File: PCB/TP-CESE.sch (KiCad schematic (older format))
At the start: 39 parts, among them J1 Screw_Terminal_01x04, J3 Screw_Terminal_01x02, J4 Conn_01x05_Male, J5 test, Q1 IRF540N, Q2 IRF540N, Q3 IRF540N, Q4 IRF540N, U1 4N25, U2 4N25, U3 4N25, U4 4N25, U5 ADS1015IDGS, X1 Conn_Poncho2P_2x_20x2

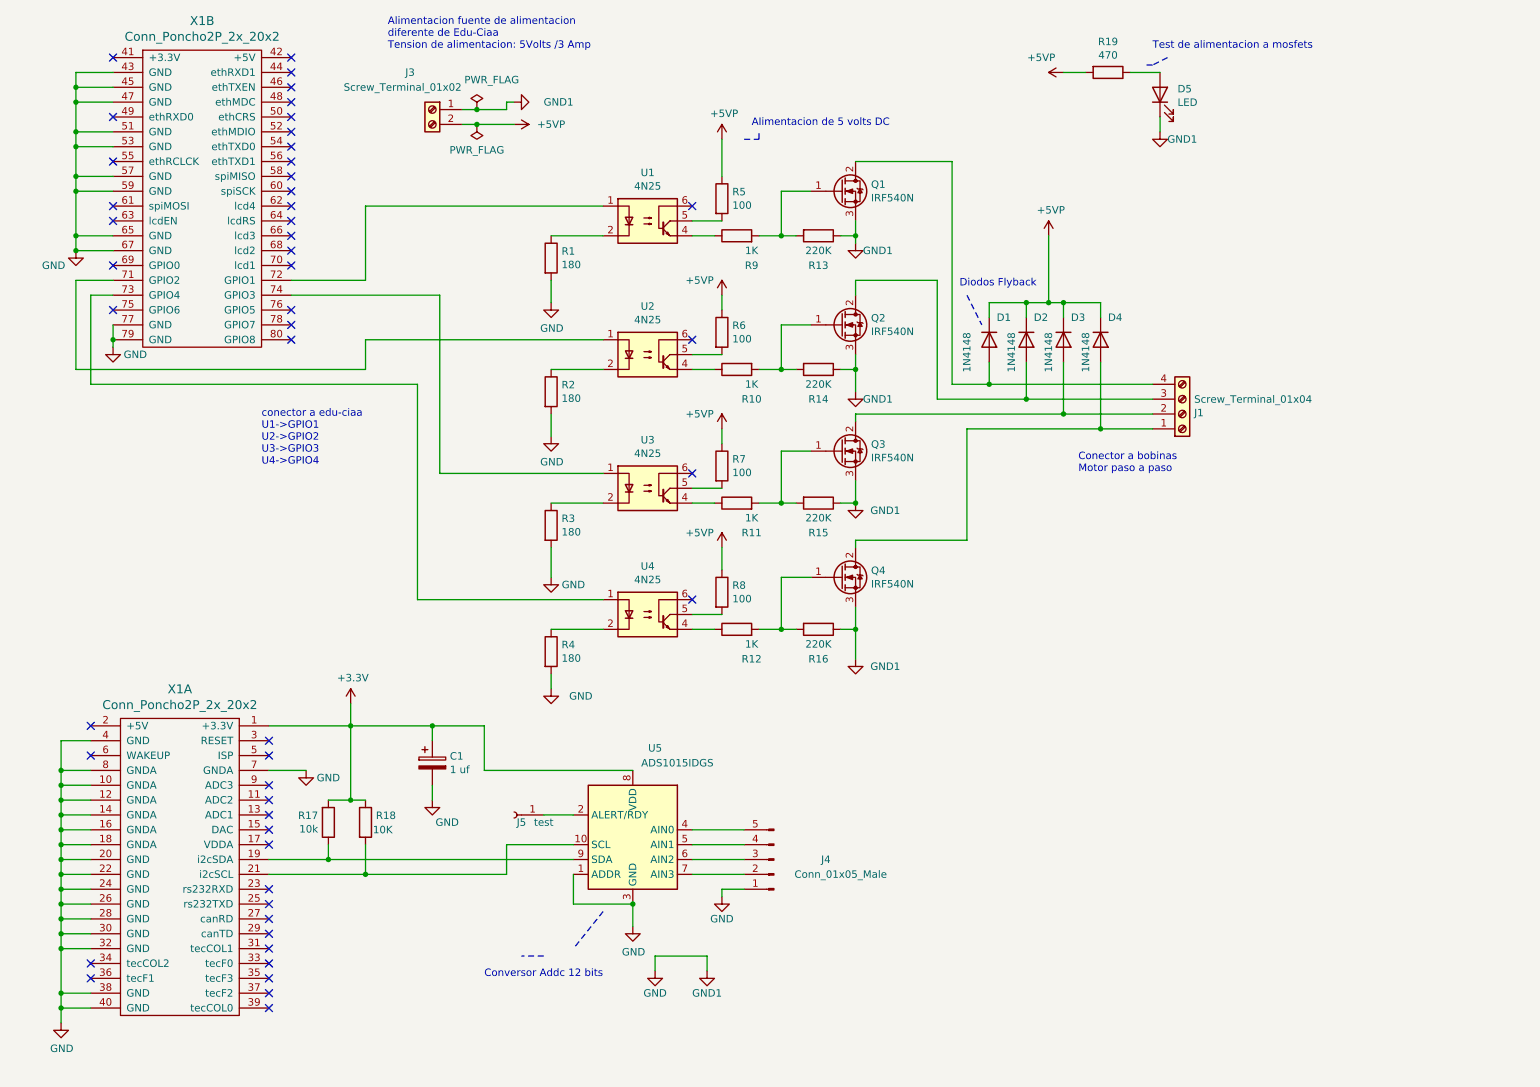
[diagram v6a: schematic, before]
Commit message: Ubicacion de componentes y ruteados
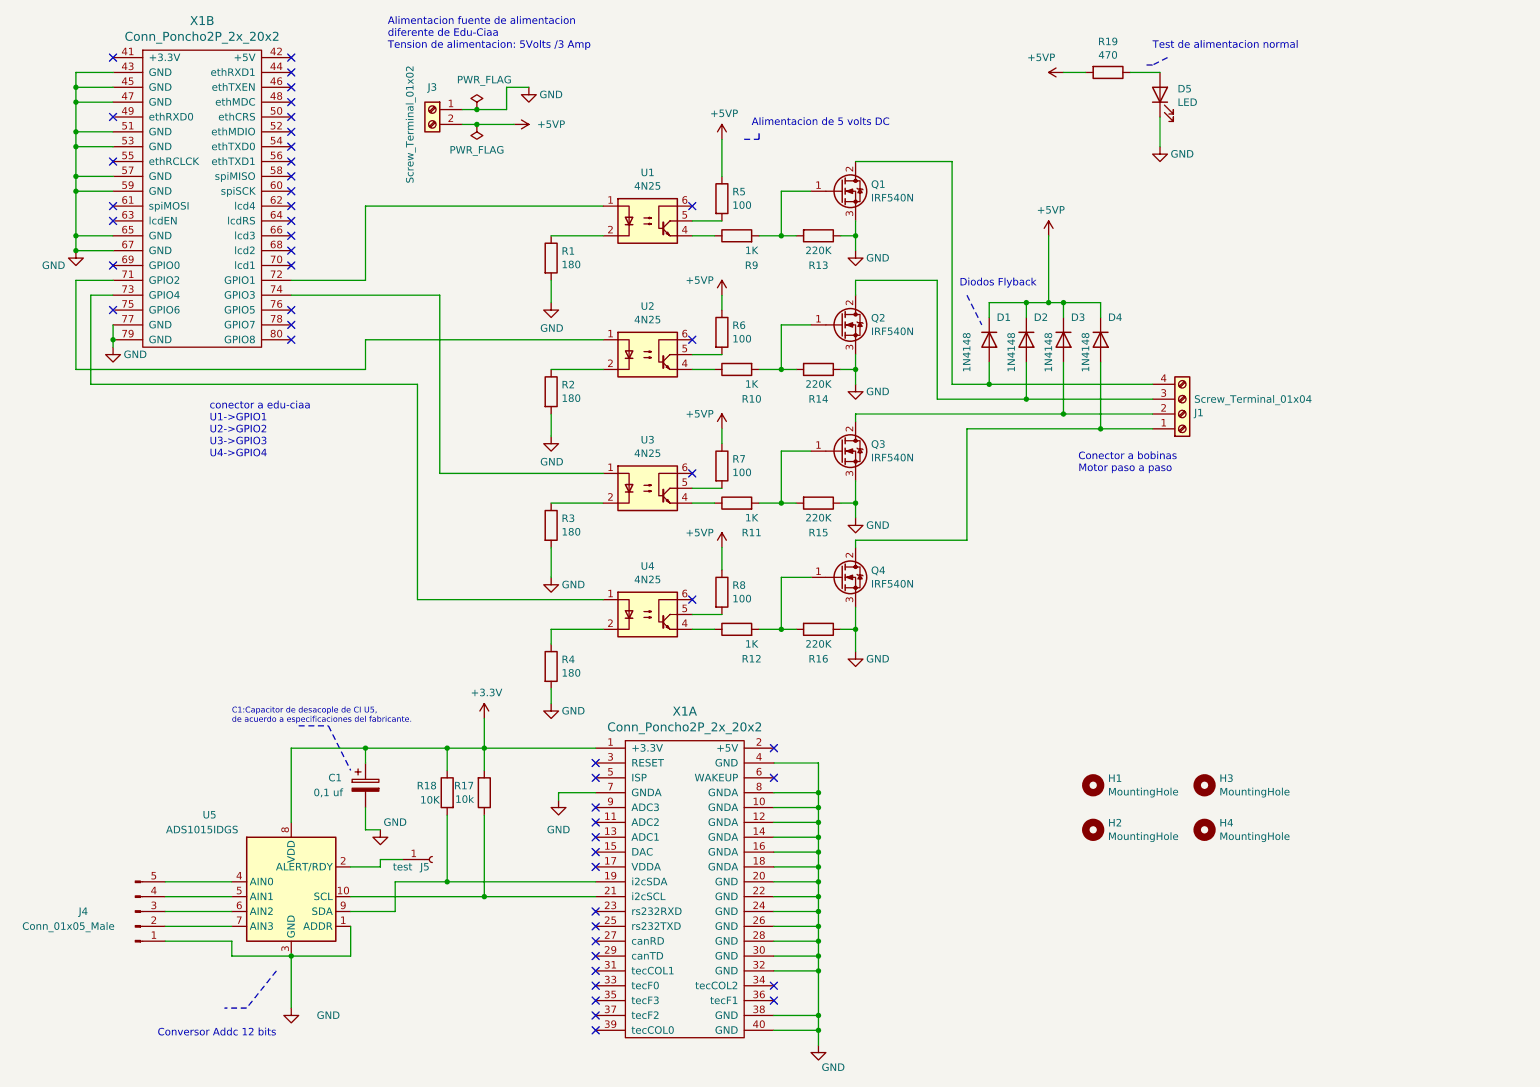
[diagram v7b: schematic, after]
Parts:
- added H1, H2, H3, H4: MountingHole, MountingHole:MountingHole_2.2mm_M2_DIN965_Pad, symbol Mechanical:MountingHole
- C1: value 1 uf -> 0,1 uf; footprint Capacitor_SMD:CP_Elec_4x4.5 -> Capacitor_SMD:C_0805_2012Metric
- D4: Digikey# (none) -> 1N4148FS-ND
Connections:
- net at U5.9 (SDA), X1.19 (i2cSDA): now also R18.2; no longer R17.1
- net at U5.10 (SCL), X1.21 (i2cSCL): now also R17.1; no longer R18.2
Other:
- note added: "C1:Capacitor de desacople de CI U5,\nde acuerdo a especificaciones del fabricante.\n\n"
- note added: "Test de alimentacion normal"
- note removed: "Test de alimentacion a mosfets"
- moved on the sheet: C1, J4, J5, R17, R18, R4, U5, X1A

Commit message: Gerbers, Bom ,mejoro conexiones
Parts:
- added FID1, FID2, FID3: Fiducial, Fiducial:Fiducial_1mm_Mask2mm, symbol Mechanical:Fiducial
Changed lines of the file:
@@
 Wire Wire Line
 	3000 6000 3100 6000
+$Comp
+L Mechanical:Fiducial FID2
+U 1 1 5FA19856
+P 9900 5500
+F 0 "FID2" H 9985 5546 50  0000 L CNN
+F 1 "Fiducial" H 9985 5455 50  0000 L CNN
+F 2 "Fiducial:Fiducial_1mm_Mask2mm" H 9900 5500 50  0001 C CNN
+F 3 "~" H 9900 5500 50  0001 C CNN
+	1    9900 5500
+	1    0    0    -1
+$EndComp
+$Comp
+L Mechanical:Fiducial FID3
+U 1 1 5FA1A33A
+P 10350 5500
+F 0 "FID3" H 10435 5546 50  0000 L CNN
+F 1 "Fiducial" H 10435 5455 50  0000 L CNN
+F 2 "Fiducial:Fiducial_1mm_Mask2mm" H 10350 5500 50  0001 C CNN
+F 3 "~" H 10350 5500 50  0001 C CNN
+	1    10350 5500
+	1    0    0    -1
+$EndComp
+$Comp
+L Mechanical:Fiducial FID1
+U 1 1 5FA1AA16
+P 9900 5750
+F 0 "FID1" H 9985 5796 50  0000 L CNN
+F 1 "Fiducial" H 9985 5705 50  0000 L CNN
+F 2 "Fiducial:Fiducial_1mm_Mask2mm" H 9900 5750 50  0001 C CNN
+F 3 "~" H 9900 5750 50  0001 C CNN
+	1    9900 5750
+	1    0    0    -1
+$EndComp
 $EndSCHEMATC
